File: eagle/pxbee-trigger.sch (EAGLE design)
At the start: 21 parts, among them J1 5452153, J2 1963599, K1 APAN3103, K2 APAN3103, K3 APAN3103, K4 APAN3103, Q1 BC548BTA, Q2 BC548BTA, Q3 BC548BTA, Q4 BC548BTA

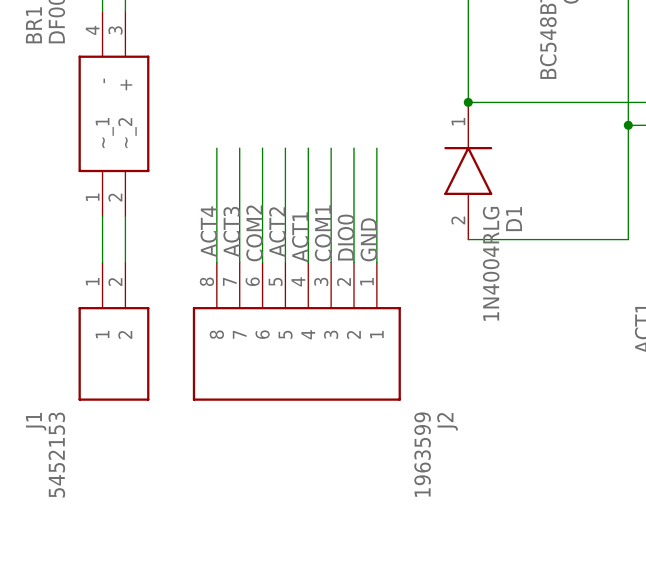
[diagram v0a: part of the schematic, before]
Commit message: Change of connector elements, smaller dimensions
- Change from Phoenix contact to 3.5mm step Molex Eurotype connectors
- Dimension the board to fit inside a small plastic conjunction box 75x75mm
- Still work in progress (WIP)
- Addresses fabrication remarks in #5
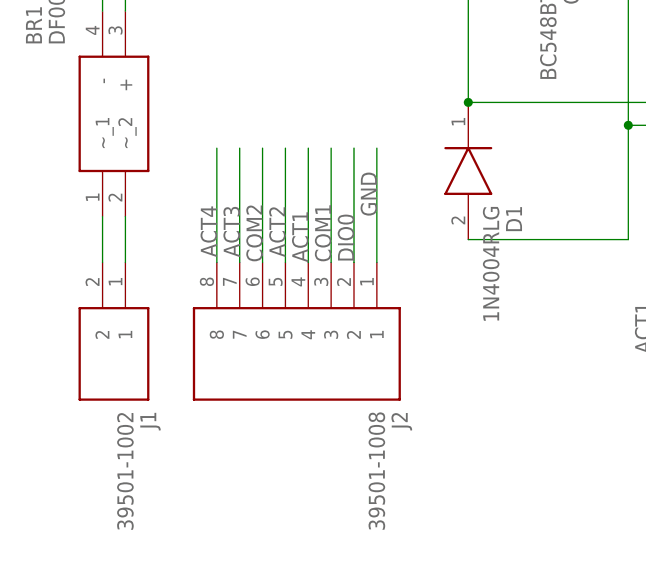
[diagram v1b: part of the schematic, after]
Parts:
- J1: value 5452153 -> 39501-1002; device parts:5452153 -> parts:39501-1002
- J2: value 1963599 -> 39501-1008; device parts:1963599 -> parts:39501-1008
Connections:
- net N$8: now also J1.2; no longer J1.1
- net N$9: now also J1.1; no longer J1.2
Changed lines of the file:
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@@
 <parts>
 <part name="FRAME1" library="frames" library_urn="urn:adsk.eagle:library:229" deviceset="A4L-LOC" device=""/>
-<part name="J1" library="parts" deviceset="5452153" device=""/>
-<part name="J2" library="parts" deviceset="1963599" device=""/>
 <part name="BR1" library="parts" deviceset="DF005M" device=""/>
 <part name="PS1" library="parts" deviceset="MGFS1R5243R3" device=""/>
@@
 <part name="D4" library="parts" deviceset="1N4004RLG" device=""/>
 <part name="R4" library="parts" deviceset="RN55D1801FB14" device=""/>
+<part name="J1" library="parts" deviceset="39501-1002" device=""/>
+<part name="J2" library="parts" deviceset="39501-1008" device=""/>
 </parts>
 <sheets>
@@
 <attribute name="SHEET" x="230.505" y="5.08" size="2.54" layer="94"/>
 </instance>
-<instance part="J1" gate="G$1" x="12.7" y="45.72" smashed="yes" rot="MR270">
-<attribute name="NAME" x="5.08" y="29.21" size="1.778" layer="95" rot="MR270" align="center-left"/>
-<attribute name="VALUE" x="7.62" y="29.21" size="1.778" layer="96" rot="MR270" align="center-left"/>
-</instance>
-<instance part="J2" gate="G$1" x="43.18" y="45.72" smashed="yes" rot="R270">
-<attribute name="NAME" x="50.8" y="29.21" size="1.778" layer="95" rot="R270" align="center-left"/>
-<attribute name="VALUE" x="48.26" y="29.21" size="1.778" layer="96" rot="R270" align="center-left"/>
-</instance>
 <instance part="BR1" gate="G$1" x="12.7" y="50.8" smashed="yes" rot="R90">
 <attribute name="NAME" x="5.08" y="69.85" size="1.778" layer="95" rot="R90" align="center-left"/>
@@
 <attribute name="NAME" x="212.09" y="100.33" size="1.778" layer="95" rot="R90" align="center-left"/>
 <attribute name="VALUE" x="214.63" y="100.33" size="1.778" layer="96" rot="R90" align="center-left"/>
+</instance>
+<instance part="J1" gate="G$1" x="15.24" y="45.72" smashed="yes" rot="R270">
+<attribute name="NAME" x="17.78" y="29.21" size="1.778" layer="95" rot="R270" align="center-left"/>
+<attribute name="VALUE" x="15.24" y="29.21" size="1.778" layer="96" rot="R270" align="center-left"/>
+</instance>
+<instance part="J2" gate="G$1" x="43.18" y="45.72" smashed="yes" rot="R270">
+<attribute name="NAME" x="45.72" y="29.21" size="1.778" layer="95" rot="R270" align="center-left"/>
+<attribute name="VALUE" x="43.18" y="29.21" size="1.778" layer="96" rot="R270" align="center-left"/>
 </instance>
 </instances>
@@
 </segment>
 <segment>
+<wire x1="43.18" y1="45.72" x2="43.18" y2="58.42" width="0.1524" layer="91"/>
+<label x="43.18" y="50.8" size="1.778" layer="95" rot="R90"/>
 <pinref part="J2" gate="G$1" pin="1"/>
-<wire x1="43.18" y1="45.72" x2="43.18" y2="58.42" width="0.1524" layer="91"/>
-<label x="43.18" y="45.72" size="1.778" layer="95" rot="R90"/>
 </segment>
 </net>
@@
 <net name="COM1" class="0">
 <segment>
-<pinref part="J2" gate="G$1" pin="3"/>
 <wire x1="38.1" y1="45.72" x2="38.1" y2="58.42" width="0.1524" layer="91"/>
 <label x="38.1" y="45.72" size="1.778" layer="95" rot="R90"/>
+<pinref part="J2" gate="G$1" pin="3"/>
 </segment>
 <segment>
@@
 <net name="ACT1" class="0">
 <segment>
-<pinref part="J2" gate="G$1" pin="4"/>
 <wire x1="35.56" y1="45.72" x2="35.56" y2="58.42" width="0.1524" layer="91"/>
 <label x="35.56" y="45.72" size="1.778" layer="95" rot="R90"/>
+<pinref part="J2" gate="G$1" pin="4"/>
 </segment>
 <segment>
@@
 <net name="ACT2" class="0">
 <segment>
-<pinref part="J2" gate="G$1" pin="5"/>
 <wire x1="33.02" y1="45.72" x2="33.02" y2="58.42" width="0.1524" layer="91"/>
 <label x="31.242" y="52.07" size="1.778" layer="95" rot="R270"/>
+<pinref part="J2" gate="G$1" pin="5"/>
 </segment>
 <segment>
@@
 <net name="COM2" class="0">
 <segment>
-<pinref part="J2" gate="G$1" pin="6"/>
 <wire x1="30.48" y1="45.72" x2="30.48" y2="58.42" width="0.1524" layer="91"/>
 <label x="30.48" y="45.72" size="1.778" layer="95" rot="R90"/>
+<pinref part="J2" gate="G$1" pin="6"/>
 </segment>
 <segment>
@@
 <net name="ACT3" class="0">
 <segment>
-<pinref part="J2" gate="G$1" pin="7"/>
 <wire x1="27.94" y1="45.72" x2="27.94" y2="58.42" width="0.1524" layer="91"/>
 <label x="26.162" y="52.07" size="1.778" layer="95" rot="R270"/>
+<pinref part="J2" gate="G$1" pin="7"/>
 </segment>
 <segment>
@@
 <net name="ACT4" class="0">
 <segment>
-<pinref part="J2" gate="G$1" pin="8"/>
 <wire x1="25.4" y1="45.72" x2="25.4" y2="58.42" width="0.1524" layer="91"/>
 <label x="23.622" y="52.07" size="1.778" layer="95" rot="R270"/>
+<pinref part="J2" gate="G$1" pin="8"/>
 </segment>
 <segment>
@@
 <net name="DIO0" class="0">
 <segment>
-<pinref part="J2" gate="G$1" pin="2"/>
 <wire x1="40.64" y1="45.72" x2="40.64" y2="58.42" width="0.1524" layer="91"/>
 <label x="40.64" y="45.72" size="1.778" layer="95" rot="R90"/>
+<pinref part="J2" gate="G$1" pin="2"/>
 </segment>
 <segment>
@@
 <segment>
 <pinref part="BR1" gate="G$1" pin="~_1"/>
+<wire x1="12.7" y1="50.8" x2="12.7" y2="45.72" width="0.1524" layer="91"/>
+<pinref part="J1" gate="G$1" pin="2"/>
+</segment>
+</net>
+<net name="N$9" class="0">
+<segment>
+<pinref part="BR1" gate="G$1" pin="~_2"/>
+<wire x1="15.24" y1="50.8" x2="15.24" y2="45.72" width="0.1524" layer="91"/>
 <pinref part="J1" gate="G$1" pin="1"/>
-<wire x1="12.7" y1="50.8" x2="12.7" y2="45.72" width="0.1524" layer="91"/>
-</segment>
-</net>
-<net name="N$9" class="0">
-<segment>
-<pinref part="BR1" gate="G$1" pin="~_2"/>
-<pinref part="J1" gate="G$1" pin="2"/>
-<wire x1="15.24" y1="50.8" x2="15.24" y2="45.72" width="0.1524" layer="91"/>
-</segment>
-</net>
+</segment>
+</net>

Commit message: Board routed; Updated parts library
- Freed pin 20, using pin 4 for gate/door status input
- Addresses findings in #5
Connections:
- removed net DIO0: J2.2, XB1.AD0/DIO0
- new net DIO12: J2.2, XB1.DIO12
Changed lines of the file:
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@@
-</segment>
-</net>
-<net name="DIO0" class="0">
-<segment>
-<wire x1="40.64" y1="45.72" x2="40.64" y2="58.42" width="0.1524" layer="91"/>
-<label x="40.64" y="45.72" size="1.778" layer="95" rot="R90"/>
-<pinref part="J2" gate="G$1" pin="2"/>
-</segment>
-<segment>
-<pinref part="XB1" gate="G$1" pin="AD0/DIO0"/>
-<wire x1="60.96" y1="139.7" x2="60.96" y2="129.54" width="0.1524" layer="91"/>
 </segment>
 </net>
@@
 </segment>
 </net>
+<net name="DIO12" class="0">
+<segment>
+<wire x1="40.64" y1="45.72" x2="40.64" y2="58.42" width="0.1524" layer="91"/>
+<label x="40.64" y="45.72" size="1.778" layer="95" rot="R90"/>
+<pinref part="J2" gate="G$1" pin="2"/>
+</segment>
+<segment>
+<pinref part="XB1" gate="G$1" pin="DIO12"/>
+<wire x1="20.32" y1="139.7" x2="20.32" y2="129.54" width="0.1524" layer="91"/>
+<label x="17.78" y="127" size="1.778" layer="95"/>
+</segment>
+</net>

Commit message: Board dimension changes
- Dimensioned to 75x75mm
- 9 pin terminal block used to gain one more status pin
- Parts library updated (removed unused parts, added new ones)
- Addresses findings in #5
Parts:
- J2: value 39501-1008 -> 39501-1009; device parts:39501-1008 -> parts:39501-1009
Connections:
- new net DIO3: J2.2, XB1.AD3/DIO3
- net ACT1: now also J2.5; no longer J2.4
- net ACT2: now also J2.6; no longer J2.5
- net ACT3: now also J2.8; no longer J2.7
- net ACT4: now also J2.9; no longer J2.8
- net COM1: now also J2.4; no longer J2.3
- net COM2: now also J2.7; no longer J2.6
- net DIO12: now also J2.3; no longer J2.2
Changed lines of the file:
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@@
 <part name="R4" library="parts" deviceset="RN55D1801FB14" device=""/>
 <part name="J1" library="parts" deviceset="39501-1002" device=""/>
-<part name="J2" library="parts" deviceset="39501-1008" device=""/>
+<part name="J2" library="parts" deviceset="39501-1009" device=""/>
 </parts>
 <sheets>
@@
 <attribute name="VALUE" x="15.24" y="29.21" size="1.778" layer="96" rot="R270" align="center-left"/>
 </instance>
-<instance part="J2" gate="G$1" x="43.18" y="45.72" smashed="yes" rot="R270">
-<attribute name="NAME" x="45.72" y="29.21" size="1.778" layer="95" rot="R270" align="center-left"/>
-<attribute name="VALUE" x="43.18" y="29.21" size="1.778" layer="96" rot="R270" align="center-left"/>
+<instance part="J2" gate="G$1" x="45.72" y="45.72" smashed="yes" rot="R270">
+<attribute name="NAME" x="48.26" y="29.21" size="1.778" layer="95" rot="R270" align="center-left"/>
+<attribute name="VALUE" x="45.72" y="29.21" size="1.778" layer="96" rot="R270" align="center-left"/>
 </instance>
 </instances>
@@
 </segment>
 <segment>
-<wire x1="43.18" y1="45.72" x2="43.18" y2="58.42" width="0.1524" layer="91"/>
-<label x="43.18" y="50.8" size="1.778" layer="95" rot="R90"/>
 <pinref part="J2" gate="G$1" pin="1"/>
+<wire x1="45.72" y1="45.72" x2="45.72" y2="58.42" width="0.1524" layer="91"/>
+<label x="45.72" y="45.72" size="1.778" layer="95" rot="R90"/>
 </segment>
 </net>
@@
 <wire x1="38.1" y1="45.72" x2="38.1" y2="58.42" width="0.1524" layer="91"/>
 <label x="38.1" y="45.72" size="1.778" layer="95" rot="R90"/>
-<pinref part="J2" gate="G$1" pin="3"/>
+<pinref part="J2" gate="G$1" pin="4"/>
 </segment>
 <segment>
@@
 <wire x1="35.56" y1="45.72" x2="35.56" y2="58.42" width="0.1524" layer="91"/>
 <label x="35.56" y="45.72" size="1.778" layer="95" rot="R90"/>
-<pinref part="J2" gate="G$1" pin="4"/>
+<pinref part="J2" gate="G$1" pin="5"/>
 </segment>
 <segment>
@@
 <wire x1="33.02" y1="45.72" x2="33.02" y2="58.42" width="0.1524" layer="91"/>
 <label x="31.242" y="52.07" size="1.778" layer="95" rot="R270"/>
-<pinref part="J2" gate="G$1" pin="5"/>
+<pinref part="J2" gate="G$1" pin="6"/>
 </segment>
 <segment>
@@
 <wire x1="30.48" y1="45.72" x2="30.48" y2="58.42" width="0.1524" layer="91"/>
 <label x="30.48" y="45.72" size="1.778" layer="95" rot="R90"/>
-<pinref part="J2" gate="G$1" pin="6"/>
+<pinref part="J2" gate="G$1" pin="7"/>
 </segment>
 <segment>
@@
 <wire x1="27.94" y1="45.72" x2="27.94" y2="58.42" width="0.1524" layer="91"/>
 <label x="26.162" y="52.07" size="1.778" layer="95" rot="R270"/>
-<pinref part="J2" gate="G$1" pin="7"/>
+<pinref part="J2" gate="G$1" pin="8"/>
 </segment>
 <segment>
@@
 <wire x1="25.4" y1="45.72" x2="25.4" y2="58.42" width="0.1524" layer="91"/>
 <label x="23.622" y="52.07" size="1.778" layer="95" rot="R270"/>
-<pinref part="J2" gate="G$1" pin="8"/>
+<pinref part="J2" gate="G$1" pin="9"/>
 </segment>
 <segment>
@@
 <wire x1="40.64" y1="45.72" x2="40.64" y2="58.42" width="0.1524" layer="91"/>
 <label x="40.64" y="45.72" size="1.778" layer="95" rot="R90"/>
-<pinref part="J2" gate="G$1" pin="2"/>
+<pinref part="J2" gate="G$1" pin="3"/>
 </segment>
 <segment>
@@
 </segment>
 </net>
+<net name="DIO3" class="0">
+<segment>
+<pinref part="J2" gate="G$1" pin="2"/>
+<wire x1="43.18" y1="45.72" x2="43.18" y2="58.42" width="0.1524" layer="91"/>
+<label x="43.18" y="45.72" size="1.778" layer="95" rot="R90"/>
+</segment>
+<segment>
+<pinref part="XB1" gate="G$1" pin="AD3/DIO3"/>
+<wire x1="53.34" y1="139.7" x2="53.34" y2="129.54" width="0.1524" layer="91"/>
+<label x="48.26" y="127" size="1.778" layer="95"/>
+</segment>
+</net>

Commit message: PCB Board changes
- Ready for fabrication v0.1.2-pcbfab.1
- Addresses findings in #5
- New pin assignment from XBee side to accommodate GPIO interrupt usage
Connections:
- removed net DIO12: J2.3, XB1.DIO12
- removed net DIO3: J2.2, XB1.AD3/DIO3
- new net DIO1: J2.3, XB1.AD1/DIO1
- new net DIO2: J2.2, XB1.AD2/DIO2
- net N$14: now also XB1.RSSI/PWM/DIO10; no longer XB1.AD1/DIO1
- net N$15: now also XB1.DIO12; no longer XB1.AD2/DIO2
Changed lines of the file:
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@@
 <pinref part="R2" gate="G$1" pin="2"/>
 <wire x1="111.76" y1="119.38" x2="111.76" y2="111.76" width="0.1524" layer="91"/>
-<pinref part="XB1" gate="G$1" pin="AD1/DIO1"/>
-<wire x1="111.76" y1="119.38" x2="58.42" y2="119.38" width="0.1524" layer="91"/>
-<wire x1="58.42" y1="119.38" x2="58.42" y2="139.7" width="0.1524" layer="91"/>
+<wire x1="111.76" y1="119.38" x2="25.4" y2="119.38" width="0.1524" layer="91"/>
+<pinref part="XB1" gate="G$1" pin="RSSI/PWM/DIO10"/>
+<wire x1="25.4" y1="119.38" x2="25.4" y2="139.7" width="0.1524" layer="91"/>
 </segment>
 </net>
@@
 <pinref part="R3" gate="G$1" pin="2"/>
 <wire x1="160.02" y1="121.92" x2="160.02" y2="111.76" width="0.1524" layer="91"/>
-<pinref part="XB1" gate="G$1" pin="AD2/DIO2"/>
-<wire x1="160.02" y1="121.92" x2="55.88" y2="121.92" width="0.1524" layer="91"/>
-<wire x1="55.88" y1="121.92" x2="55.88" y2="139.7" width="0.1524" layer="91"/>
+<wire x1="160.02" y1="121.92" x2="20.32" y2="121.92" width="0.1524" layer="91"/>
+<pinref part="XB1" gate="G$1" pin="DIO12"/>
+<wire x1="20.32" y1="121.92" x2="20.32" y2="139.7" width="0.1524" layer="91"/>
 </segment>
 </net>
@@
 </segment>
 </net>
-<net name="DIO12" class="0">
+<net name="DIO2" class="0">
+<segment>
+<pinref part="XB1" gate="G$1" pin="AD2/DIO2"/>
+<wire x1="55.88" y1="139.7" x2="55.88" y2="129.54" width="0.1524" layer="91"/>
+<label x="50.8" y="127" size="1.778" layer="95"/>
+</segment>
+<segment>
+<pinref part="J2" gate="G$1" pin="2"/>
+<wire x1="43.18" y1="45.72" x2="43.18" y2="58.42" width="0.1524" layer="91"/>
+<label x="43.18" y="45.72" size="1.778" layer="95" rot="R90"/>
+</segment>
+</net>
+<net name="DIO1" class="0">
+<segment>
+<pinref part="XB1" gate="G$1" pin="AD1/DIO1"/>
+<wire x1="58.42" y1="139.7" x2="58.42" y2="129.54" width="0.1524" layer="91"/>
+<label x="58.42" y="127" size="1.778" layer="95"/>
+</segment>
 <segment>
 <wire x1="40.64" y1="45.72" x2="40.64" y2="58.42" width="0.1524" layer="91"/>
@@
 <pinref part="J2" gate="G$1" pin="3"/>
 </segment>
-<segment>
-<pinref part="XB1" gate="G$1" pin="DIO12"/>
-<wire x1="20.32" y1="139.7" x2="20.32" y2="129.54" width="0.1524" layer="91"/>
-<label x="17.78" y="127" size="1.778" layer="95"/>
-</segment>
 </net>
-<net name="DIO3" class="0">
-<segment>
-<pinref part="J2" gate="G$1" pin="2"/>
-<wire x1="43.18" y1="45.72" x2="43.18" y2="58.42" width="0.1524" layer="91"/>
-<label x="43.18" y="45.72" size="1.778" layer="95" rot="R90"/>
-</segment>
-<segment>
-<pinref part="XB1" gate="G$1" pin="AD3/DIO3"/>
-<wire x1="53.34" y1="139.7" x2="53.34" y2="129.54" width="0.1524" layer="91"/>
-<label x="48.26" y="127" size="1.778" layer="95"/>
-</segment>
-</net>
